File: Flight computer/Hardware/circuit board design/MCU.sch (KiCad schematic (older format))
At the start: 26 parts, among them J1 Conn_01x04, J5 USB_B_Micro, U11 ATSAML21J18B-MUT, U7 W74M64FV, Y2 32.768KHz, Y3 16MHz

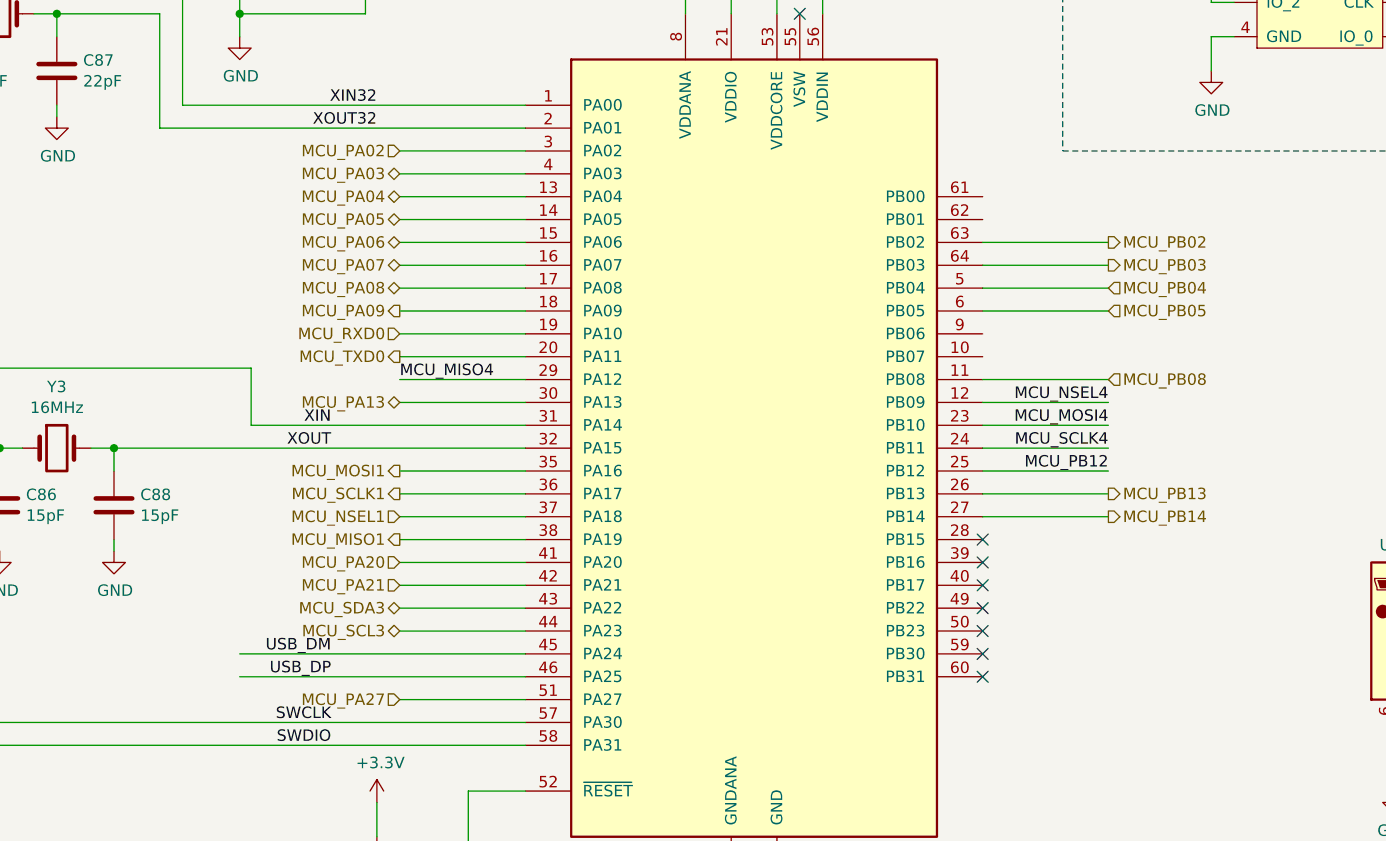
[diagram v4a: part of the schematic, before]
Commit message: connected 4 channels of pyro drivers
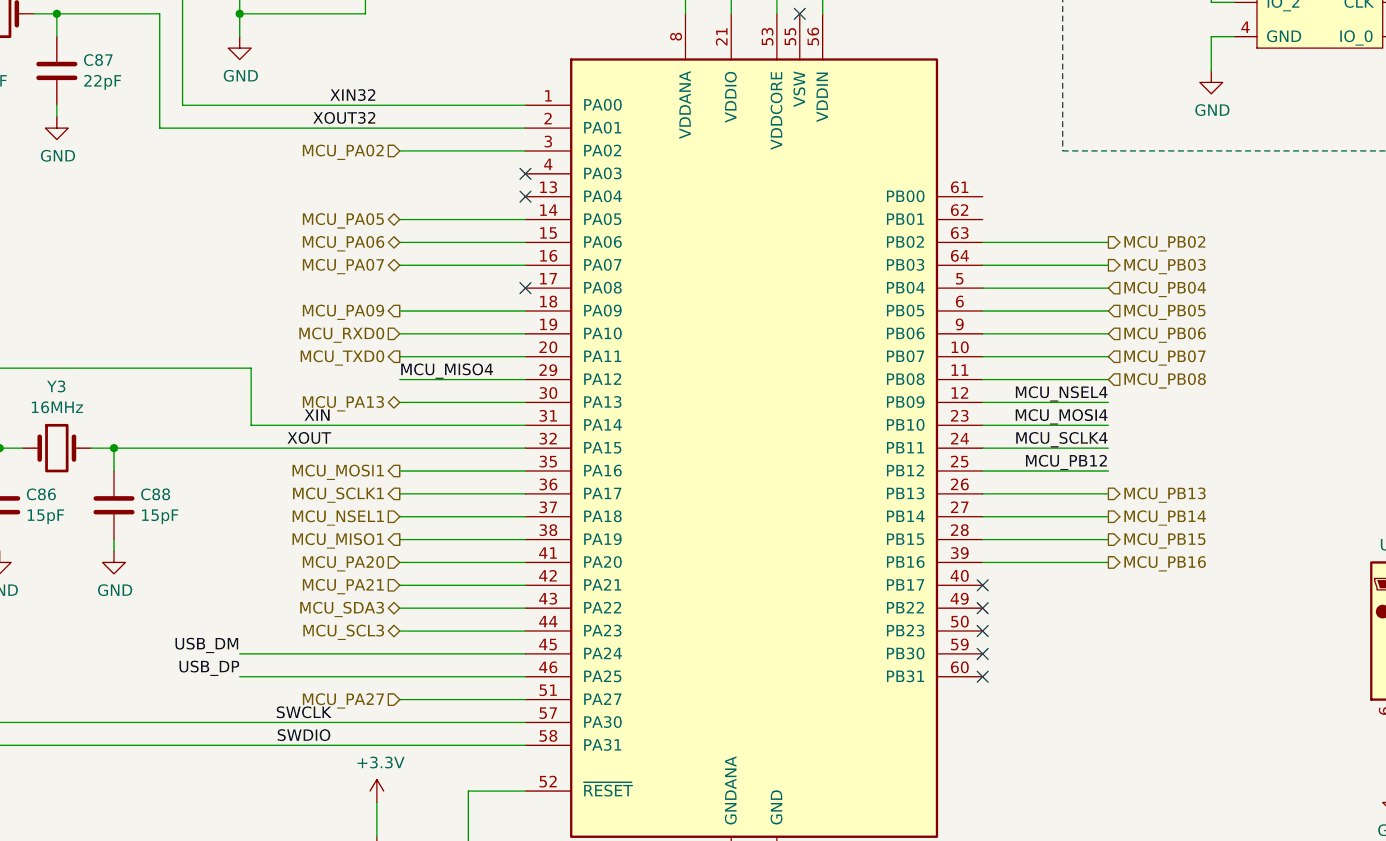
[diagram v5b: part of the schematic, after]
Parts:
- J5: footprint (none) -> Connector_USB:USB_Micro-B_Molex-105017-0001
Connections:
- net MCU_PB07: now reaches U11.10 (PB07)
- net MCU_PB15: now reaches U11.28 (PB15)
- net MCU_PB16: now reaches U11.39 (PB16)
- net MCU_PB06: now reaches U11.9 (PB06)
- net MCU_PA03: no longer names the net of U11.4 (PA03)
- net MCU_PA04: no longer names the net of U11.13 (PA04)
- net MCU_PA08: no longer names the net of U11.17 (PA08)
- no-connect marks 9 -> 10
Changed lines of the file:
@@
 Text Label 4250 4400 2    50   ~ 0
 XOUT
-Text Label 4250 5600 2    50   ~ 0
-SWCLK
 Text Label 4250 5700 2    50   ~ 0
 SWDIO
-Text Label 4250 5300 2    50   ~ 0
+Text Label 3850 5300 2    50   ~ 0
 USB_DM
-Text Label 4250 5400 2    50   ~ 0
+Text Label 3850 5400 2    50   ~ 0
 USB_DP
 Wire Wire Line
@@
 	8100 2600 8100 2750
 Wire Wire Line
-	5100 3200 4550 3200
-Wire Wire Line
-	5100 3300 4550 3300
-Wire Wire Line
 	5100 3400 4550 3400
 Wire Wire Line
@@
 Wire Wire Line
 	5100 3600 4550 3600
-Wire Wire Line
-	5100 3700 4550 3700
-Text HLabel 4550 3200 0    50   BiDi ~ 0
-MCU_PA03
-Text HLabel 4550 3300 0    50   BiDi ~ 0
-MCU_PA04
 Text HLabel 4550 3400 0    50   BiDi ~ 0
 MCU_PA05
@@
 Text HLabel 4550 3600 0    50   BiDi ~ 0
 MCU_PA07
-Text HLabel 4550 3700 0    50   BiDi ~ 0
-MCU_PA08
 Wire Wire Line
 	5100 3800 4550 3800
@@
 Wire Wire Line
 	4550 5000 5100 5000
-Text HLabel 4550 5500 0    50   Input ~ 0
-MCU_PA27
 Wire Wire Line
 	4550 5500 5100 5500
@@
 NoConn ~ 7100 5100
 NoConn ~ 7100 5000
-NoConn ~ 7100 4900
-NoConn ~ 7100 4800
 Wire Notes Line
 	7450 1500 7450 3100
@@
 F 0 "J5" H 9057 5667 50  0000 C CNN
 F 1 "USB_B_Micro" H 9057 5576 50  0000 C CNN
-F 2 "" H 9150 5150 50  0001 C CNN
+F 2 "Connector_USB:USB_Micro-B_Molex-105017-0001" H 9150 5150 50  0001 C CNN
 F 3 "~" H 9150 5150 50  0001 C CNN
 	1    9000 5200
@@
 Text HLabel 7650 4700 2    50   Output ~ 0
 MCU_PB14
+Wire Wire Line
+	7100 3900 7650 3900
+Wire Wire Line
+	7100 4000 7650 4000
+Text HLabel 7650 3900 2    50   Input ~ 0
+MCU_PB06
+Text HLabel 7650 4000 2    50   Input ~ 0
+MCU_PB07
+Wire Wire Line
+	7100 4800 7650 4800
+Wire Wire Line
+	7100 4900 7650 4900
+Text HLabel 7650 4800 2    50   Output ~ 0
+MCU_PB15
+Text HLabel 7650 4900 2    50   Output ~ 0
+MCU_PB16
+Text HLabel 4550 5500 0    50   Input ~ 0
+MCU_PA27
+Text Label 4250 5600 2    50   ~ 0
+SWCLK
+NoConn ~ 5100 3700
+NoConn ~ 5100 3300
+NoConn ~ 5100 3200
 $EndSCHEMATC

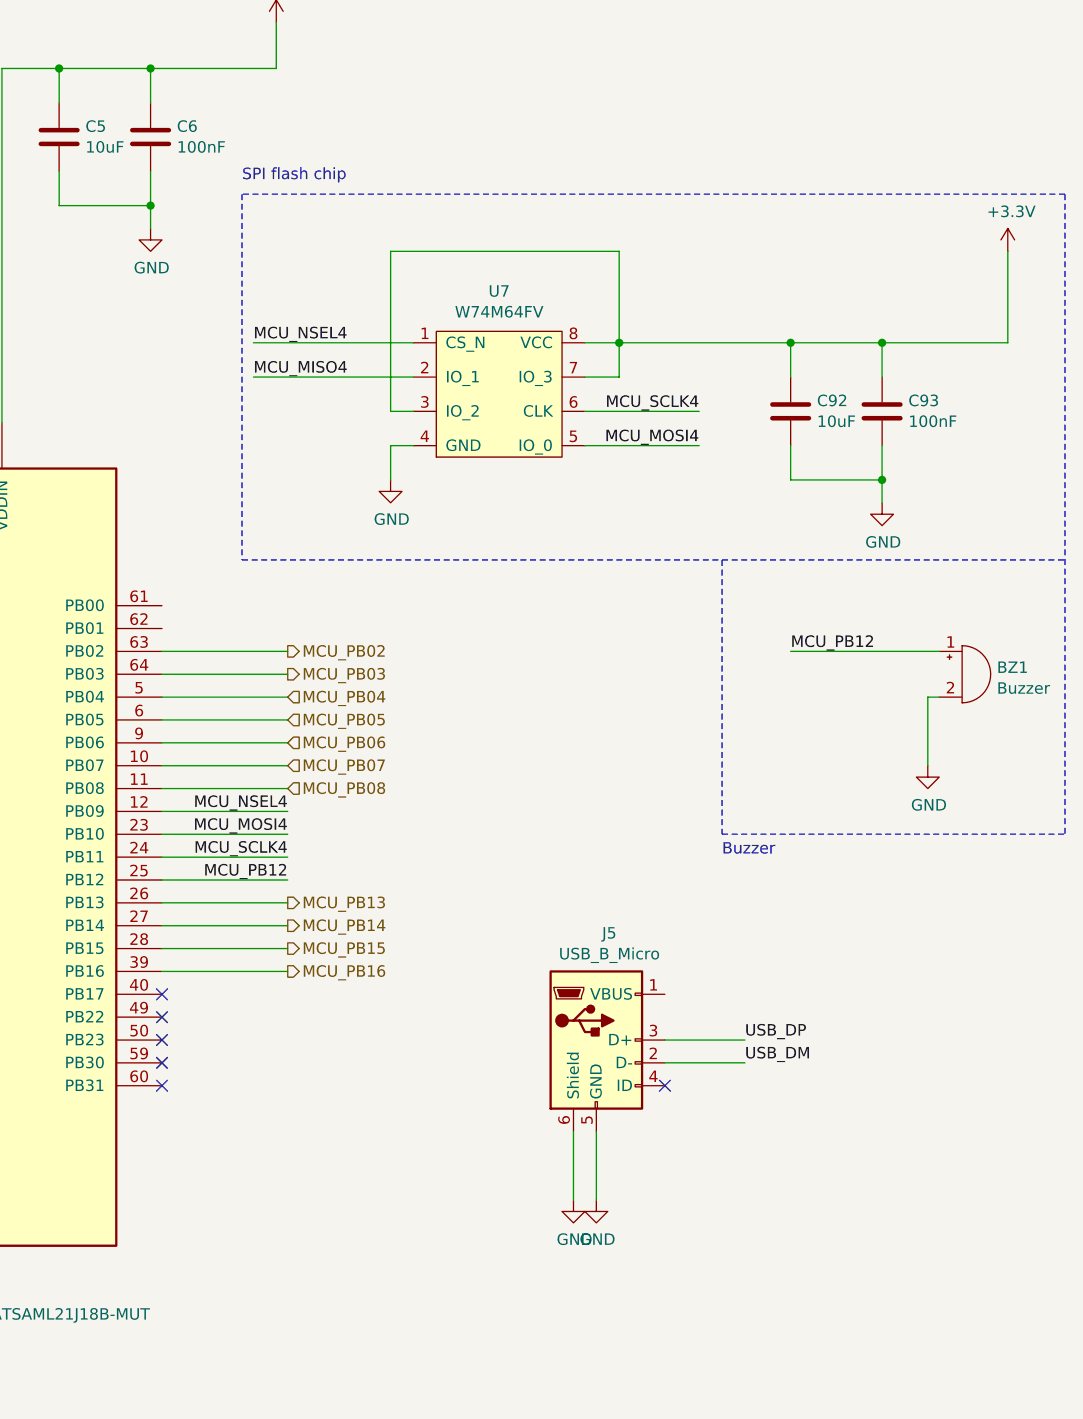
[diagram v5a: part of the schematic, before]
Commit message: put in the indicator LEDs
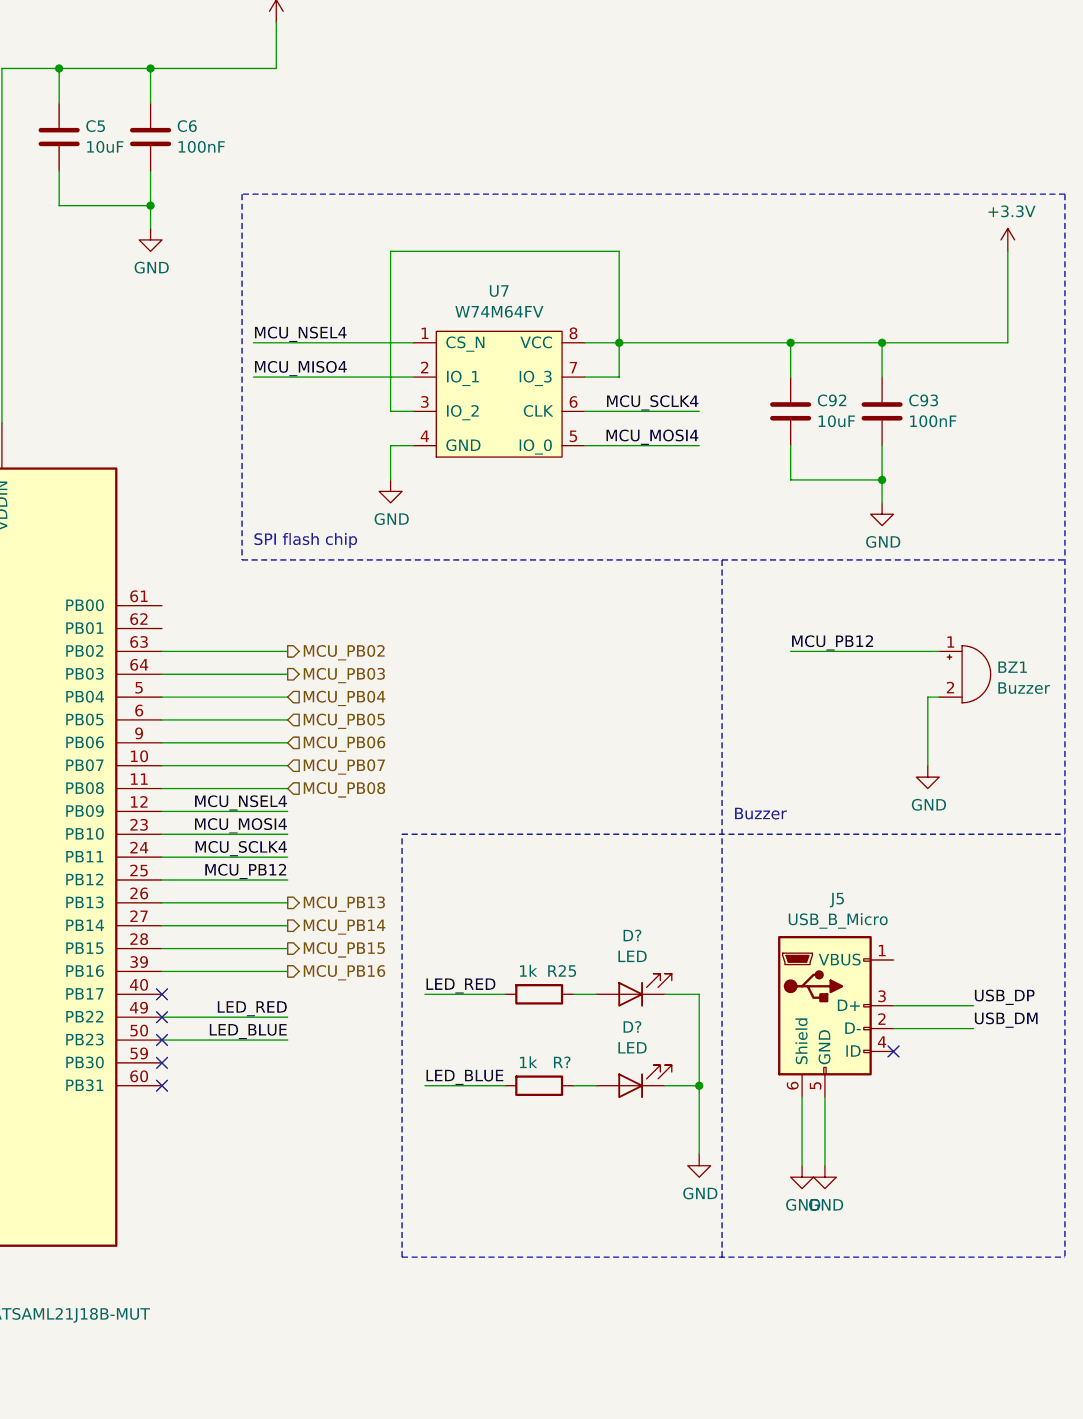
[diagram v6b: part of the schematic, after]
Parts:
- added D? (x2): LED, symbol Device:LED
- added R25, R?: 1k, symbol Device:R
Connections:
- net GND: now also D?.1 (K), D?.1 (K)
- net LED_RED: now reaches U11.49 (PB22)
- net LED_RED: now also R25.2
- net LED_BLUE: now reaches U11.50 (PB23)
- net LED_BLUE: now also R?.2
- new net: D?.2 (A), R25.1
- new net: D?.2 (A), R?.1
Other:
- moved on the sheet: J5
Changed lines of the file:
@@
 $Descr A4 11693 8268
 encoding utf-8
-Sheet 7 7
+Sheet 6 7
 Title ""
 Date ""
@@
 Wire Notes Line
 	11050 1500 7450 1500
-Text Notes 7450 1450 0    50   ~ 0
+Text Notes 7500 3050 0    50   ~ 0
 SPI flash chip
-Text Label 9650 5300 0    50   ~ 0
+Text Label 10650 5150 0    50   ~ 0
 USB_DM
-Text Label 9650 5200 0    50   ~ 0
+Text Label 10650 5050 0    50   ~ 0
 USB_DP
 Text HLabel 7650 3600 2    50   Output ~ 0
@@
 Wire Wire Line
 	7650 4400 7100 4400
-NoConn ~ 9300 5400
-Wire Wire Line
-	8900 5600 8900 5900
+NoConn ~ 10300 5250
+Wire Wire Line
+	9900 5450 9900 5750
 $Comp
 L power:GND #PWR0104
 U 1 1 5D7F3C59
-P 8900 5900
-F 0 "#PWR0104" H 8900 5650 50  0001 C CNN
-F 1 "GND" H 8905 5727 50  0000 C CNN
-F 2 "" H 8900 5900 50  0001 C CNN
-F 3 "" H 8900 5900 50  0001 C CNN
-	1    8900 5900
-	1    0    0    -1
-$EndComp
-Wire Wire Line
-	9000 5600 9000 5900
-Wire Wire Line
-	9650 5200 9300 5200
-Wire Wire Line
-	9300 5300 9650 5300
+P 9900 5750
+F 0 "#PWR0104" H 9900 5500 50  0001 C CNN
+F 1 "GND" H 9905 5577 50  0000 C CNN
+F 2 "" H 9900 5750 50  0001 C CNN
+F 3 "" H 9900 5750 50  0001 C CNN
+	1    9900 5750
+	1    0    0    -1
+$EndComp
+Wire Wire Line
+	10000 5450 10000 5750
+Wire Wire Line
+	10650 5050 10300 5050
+Wire Wire Line
+	10300 5150 10650 5150
 $Comp
 L power:GND #PWR0103
 U 1 1 5D7AB0A9
-P 9000 5900
-F 0 "#PWR0103" H 9000 5650 50  0001 C CNN
-F 1 "GND" H 9005 5727 50  0000 C CNN
-F 2 "" H 9000 5900 50  0001 C CNN
-F 3 "" H 9000 5900 50  0001 C CNN
-	1    9000 5900
-	1    0    0    -1
-$EndComp
-$Comp
-L Connector:USB_B_Micro J5
-U 1 1 5D7395BE
-P 9000 5200
-F 0 "J5" H 9057 5667 50  0000 C CNN
-F 1 "USB_B_Micro" H 9057 5576 50  0000 C CNN
-F 2 "Connector_USB:USB_Micro-B_Molex-105017-0001" H 9150 5150 50  0001 C CNN
-F 3 "~" H 9150 5150 50  0001 C CNN
-	1    9000 5200
+P 10000 5750
+F 0 "#PWR0103" H 10000 5500 50  0001 C CNN
+F 1 "GND" H 10005 5577 50  0000 C CNN
+F 2 "" H 10000 5750 50  0001 C CNN
+F 3 "" H 10000 5750 50  0001 C CNN
+	1    10000 5750
 	1    0    0    -1
 $EndComp
@@
 Text Label 7650 4500 2    50   ~ 0
 MCU_PB12
-Wire Notes Line
-	9550 4300 11050 4300
-Wire Notes Line
-	11050 1500 11050 4300
-Wire Notes Line
-	9550 3100 9550 4300
-Text Notes 9550 4400 0    50   ~ 0
+Text Notes 9600 4250 0    50   ~ 0
 Buzzer\n
 Wire Wire Line
@@
 NoConn ~ 5100 3300
 NoConn ~ 5100 3200
+$Comp
+L Device:R R25
+U 1 1 5D84A9D3
+P 8750 5000
+F 0 "R25" V 8650 5100 50  0000 C CNN
+F 1 "1k" V 8650 4950 50  0000 C CNN
+F 2 "" V 8680 5000 50  0001 C CNN
+F 3 "~" H 8750 5000 50  0001 C CNN
+	1    8750 5000
+	0    1    1    0
+$EndComp
+$Comp
+L Connector:USB_B_Micro J5
+U 1 1 5D7395BE
+P 10000 5050
+F 0 "J5" H 10057 5517 50  0000 C CNN
+F 1 "USB_B_Micro" H 10057 5426 50  0000 C CNN
+F 2 "Connector_USB:USB_Micro-B_Molex-105017-0001" H 10150 5000 50  0001 C CNN
+F 3 "~" H 10150 5000 50  0001 C CNN
+	1    10000 5050
+	1    0    0    -1
+$EndComp
+Wire Notes Line
+	11050 1500 11050 6150
+Wire Notes Line
+	9550 3100 9550 6150
+Wire Notes Line
+	8150 6150 8150 4300
+Wire Wire Line
+	9300 5000 9450 5000
+$Comp
+L Device:LED D?
+U 1 1 5D84CD91
+P 9150 5000
+F 0 "D?" H 9143 4745 50  0000 C CNN
+F 1 "LED" H 9143 4836 50  0000 C CNN
+F 2 "" H 9150 5000 50  0001 C CNN
+F 3 "~" H 9150 5000 50  0001 C CNN
+	1    9150 5000
+	-1   0    0    1
+$EndComp
+Wire Wire Line
+	8900 5000 9000 5000
+$Comp
+L Device:R R?
+U 1 1 5D8A257E
+P 8750 5400
+F 0 "R?" V 8650 5500 50  0000 C CNN
+F 1 "1k" V 8650 5350 50  0000 C CNN
+F 2 "" V 8680 5400 50  0001 C CNN
+F 3 "~" H 8750 5400 50  0001 C CNN
+	1    8750 5400
+	0    1    1    0
+$EndComp
+Wire Wire Line
+	9300 5400 9450 5400
+$Comp
+L Device:LED D?
+U 1 1 5D8A258A
+P 9150 5400
+F 0 "D?" H 9143 5145 50  0000 C CNN
+F 1 "LED" H 9143 5236 50  0000 C CNN
+F 2 "" H 9150 5400 50  0001 C CNN
+F 3 "~" H 9150 5400 50  0001 C CNN
+	1    9150 5400
+	-1   0    0    1
+$EndComp
+Wire Wire Line
+	8900 5400 9000 5400
+Wire Wire Line
+	9450 5000 9450 5400
+Connection ~ 9450 5400
+Wire Wire Line
+	9450 5400 9450 5700
+Text Label 7650 5100 2    50   ~ 0
+LED_RED
+Wire Wire Line
+	7100 5100 7650 5100
+Text Label 7650 5200 2    50   ~ 0
+LED_BLUE
+Wire Wire Line
+	7100 5200 7650 5200
+$Comp
+L power:GND #PWR?
+U 1 1 5D8CC1E1
+P 9450 5700
+F 0 "#PWR?" H 9450 5450 50  0001 C CNN
+F 1 "GND" H 9455 5527 50  0000 C CNN
+F 2 "" H 9450 5700 50  0001 C CNN
+F 3 "" H 9450 5700 50  0001 C CNN
+	1    9450 5700
+	1    0    0    -1
+$EndComp
+Text Label 8250 5000 0    50   ~ 0
+LED_RED
+Text Label 8250 5400 0    50   ~ 0
+LED_BLUE
+Wire Notes Line
+	8150 6150 11050 6150
+Wire Notes Line
+	8150 4300 11050 4300
+Wire Wire Line
+	8600 5400 8250 5400
+Wire Wire Line
+	8600 5000 8250 5000
 $EndSCHEMATC
